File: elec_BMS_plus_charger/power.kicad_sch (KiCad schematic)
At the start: 42 parts, among them J1 Conn_01x02, J13 Dynamixel-3, J14 Dynamixel-3, J2 JST SH, J7 JST SH, Q1 Q_NMOS_DGS, Q2 Q_NMOS_DGS, U1 HY2120, U2 BQ25887RGE

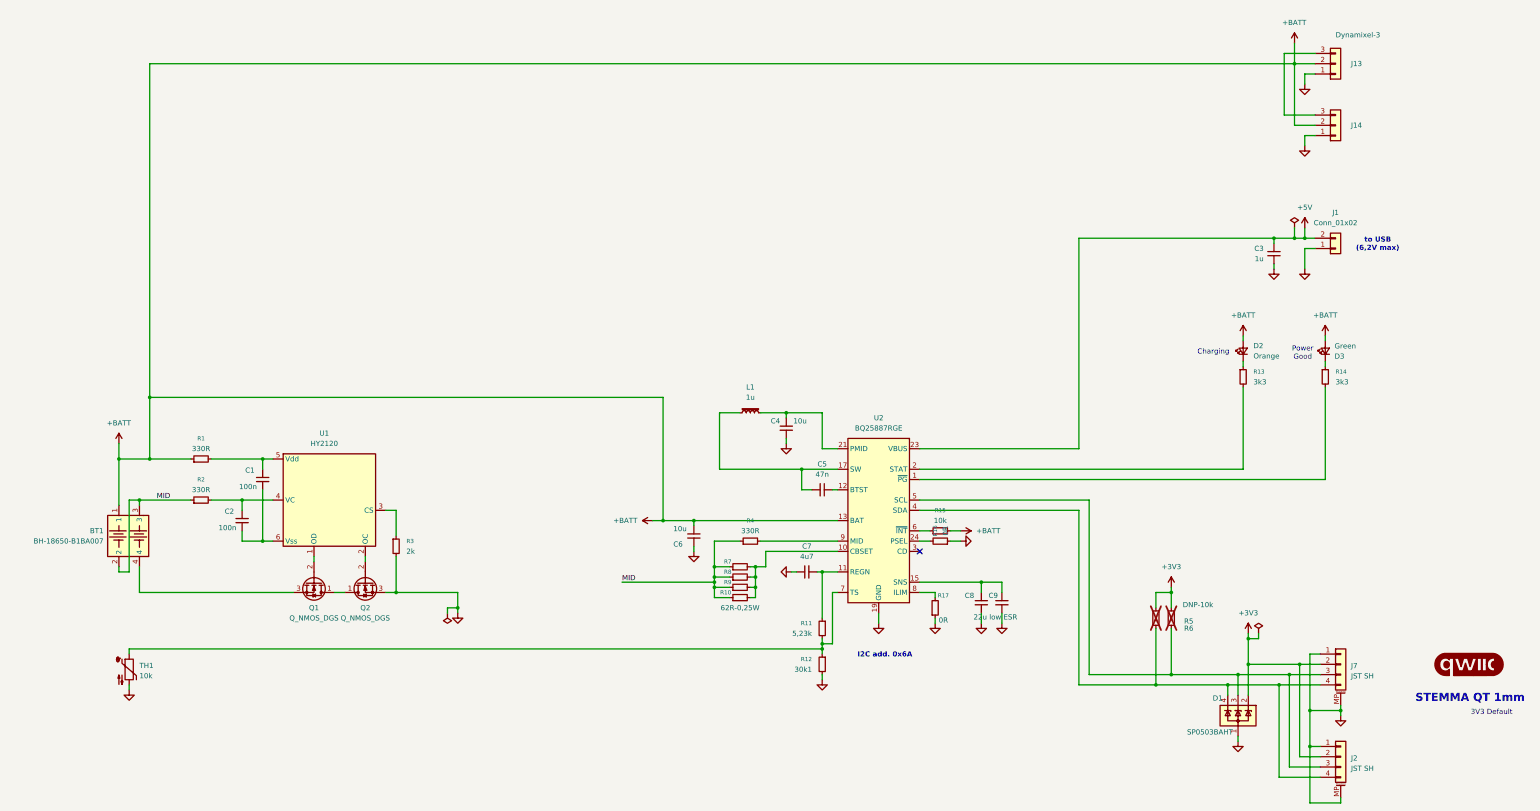
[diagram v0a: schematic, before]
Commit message: [update] BMS schematic DRC 0k.
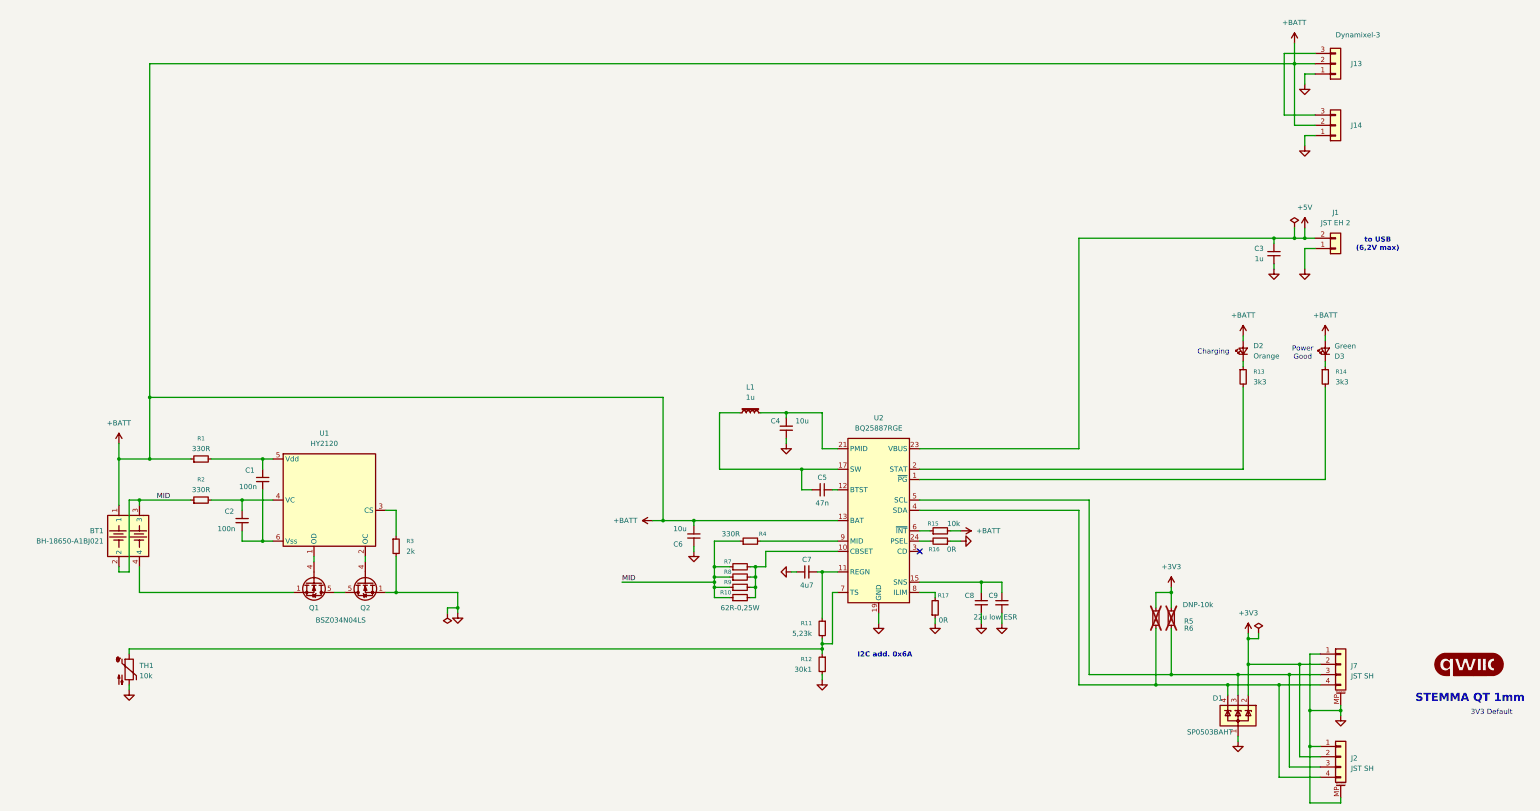
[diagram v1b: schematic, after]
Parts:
- removed Q1, Q2: Q_NMOS_DGS, symbol Transistor_FET:Q_NMOS_DGS
- added Q1, Q2: BSZ034N04LS, Library_Pollen:PQFN_3.3x3.3mm_-_PG-TDSON-8_FL, symbol Library_Pollen:BSZ034N04LS
- BT1: value BH-18650-B1BA007 -> BH-18650-A1BJ021; footprint LCSC_parts_lib:BAT-SMD_BH-18650-B1BA007 -> LCSC_parts_lib:BAT-TH_L77.0-W39.9_BH-18650-A1BJ021; LCSC Part C6937126 -> C20606804
- C3, L1: footprint (none) -> Capacitor_SMD:C_0402_1005Metric; LCSC Part (none) -> C52923
- C4, C6: footprint (none) -> Capacitor_SMD:C_0603_1608Metric; LCSC Part (none) -> C19702
- C5: footprint (none) -> Capacitor_SMD:C_0402_1005Metric; LCSC Part (none) -> C272875
- C7: footprint (none) -> Capacitor_SMD:C_0603_1608Metric; LCSC Part (none) -> C1705
- C8: footprint (none) -> Capacitor_SMD:C_0805_2012Metric; LCSC Part (none) -> C5674
- C9: value 22u -> 22u low ESR; footprint (none) -> Capacitor_SMD:C_0805_2012Metric; LCSC Part (none) -> C5674
- D2: footprint (none) -> LED_SMD:LED_0603_1608Metric; LCSC Part (none) -> C84269
- J1: value Conn_01x02 -> JST EH 2; footprint (none) -> Connector_JST:JST_EH_B2B-EH-A_1x02_P2.50mm_Vertical; LCSC Part (none) -> C160262
- J2, J7: footprint Connector_JST:JST_SH_SM04B-SRSS-TB_1x04-1MP_P1.00mm_Horizontal -> Connector_JST:JST_SH_BM04B-SRSS-TB_1x04-1MP_P1.00mm_Vertical; LCSC Part C160404 -> C160390
- R1, R2, R4: LCSC Part (none) -> C25104
- R10, R7, R8, R9: footprint (none) -> Resistor_SMD:R_1206_3216Metric; LCSC Part (none) -> C3013271
- R11: footprint (none) -> Resistor_SMD:R_0402_1005Metric; LCSC Part (none) -> C2933105
- R12: footprint (none) -> Resistor_SMD:R_0402_1005Metric; LCSC Part (none) -> C2998131
- R13, R14: footprint (none) -> Resistor_SMD:R_0402_1005Metric; LCSC Part (none) -> C25890
- R15, TH1: footprint (none) -> Resistor_SMD:R_0402_1005Metric; LCSC Part (none) -> C2906861
- R3: footprint (none) -> Resistor_SMD:R_0402_1005Metric; LCSC Part (none) -> C2909344
- R5, R6: LCSC Part C25744 -> (none)
- U2: LCSC Part (none) -> C2761614; Man. (none) -> TI; Man. Ref. (none) -> BQ25887RGER
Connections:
- net GND: now also Q2.1 (S)
- net at BT1.4: now also Q1.1 (S)
- net at U1.2 (OC): now also Q2.4 (G)
- net at U1.1 (OD): now also Q1.4 (G)
- new net: Q1.5 (D), Q2.5 (D)

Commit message: [update] Mechanical adaptations.
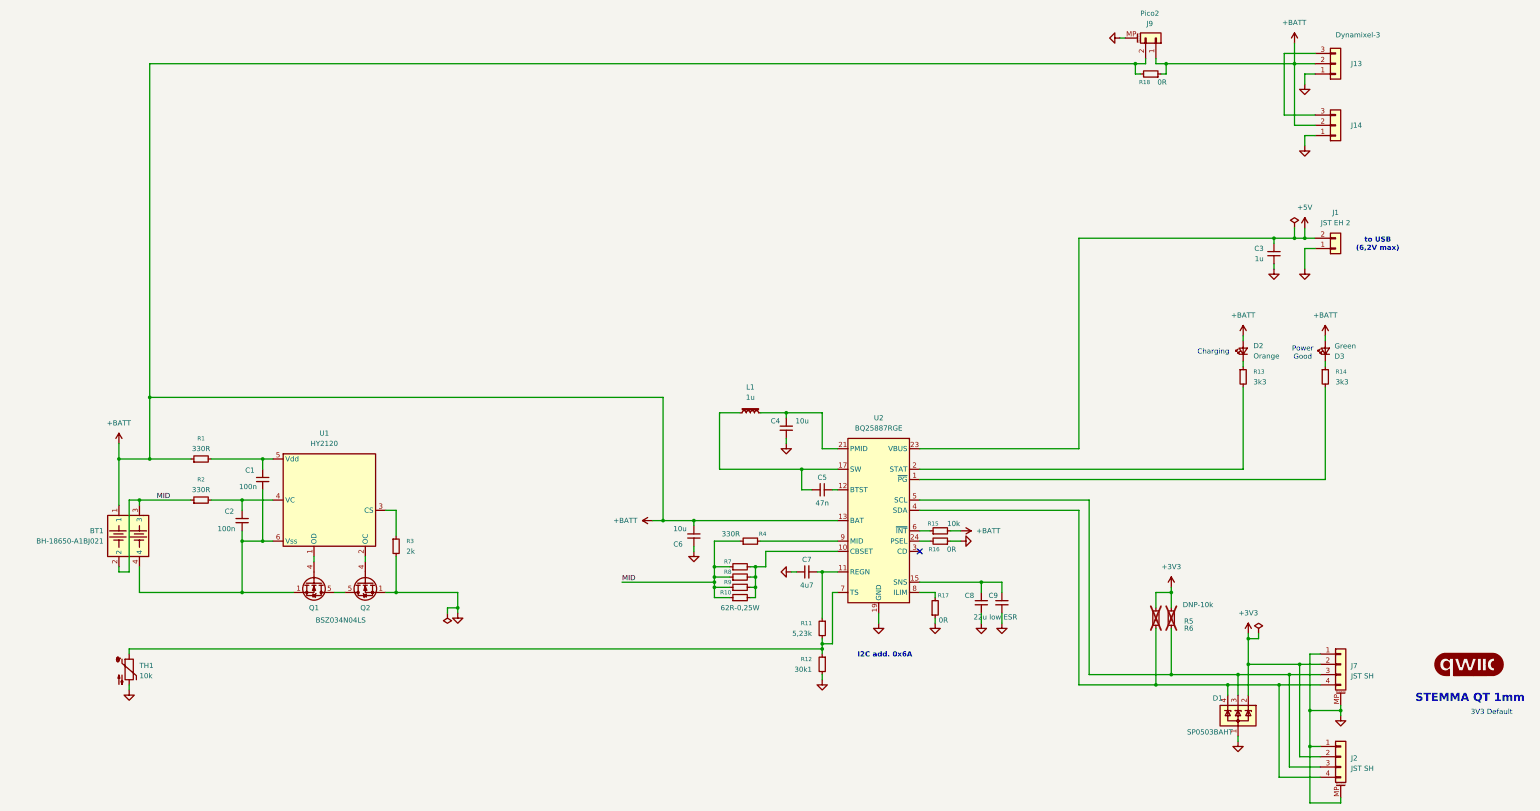
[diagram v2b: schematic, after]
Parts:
- added J9: Pico2, Connector_Molex:Molex_PicoBlade_53047-0210_1x02_P1.25mm_Vertical, symbol Connector_Generic_MountingPin:Conn_01x02_MountingPin
- added R18: 0R, Resistor_SMD:R_0603_1608Metric, symbol Device:R_Small
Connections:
- net +BATT: now also J9.1 (Pin_1), J9.2 (Pin_2), R18.1, R18.2
- net GND: now also J9.MP (MountPin)
- net at BT1.4, Q1.1 (S): now also C1.2, C2.2, U1.6 (Vss)

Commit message: [update] BMS+charger DRC OK
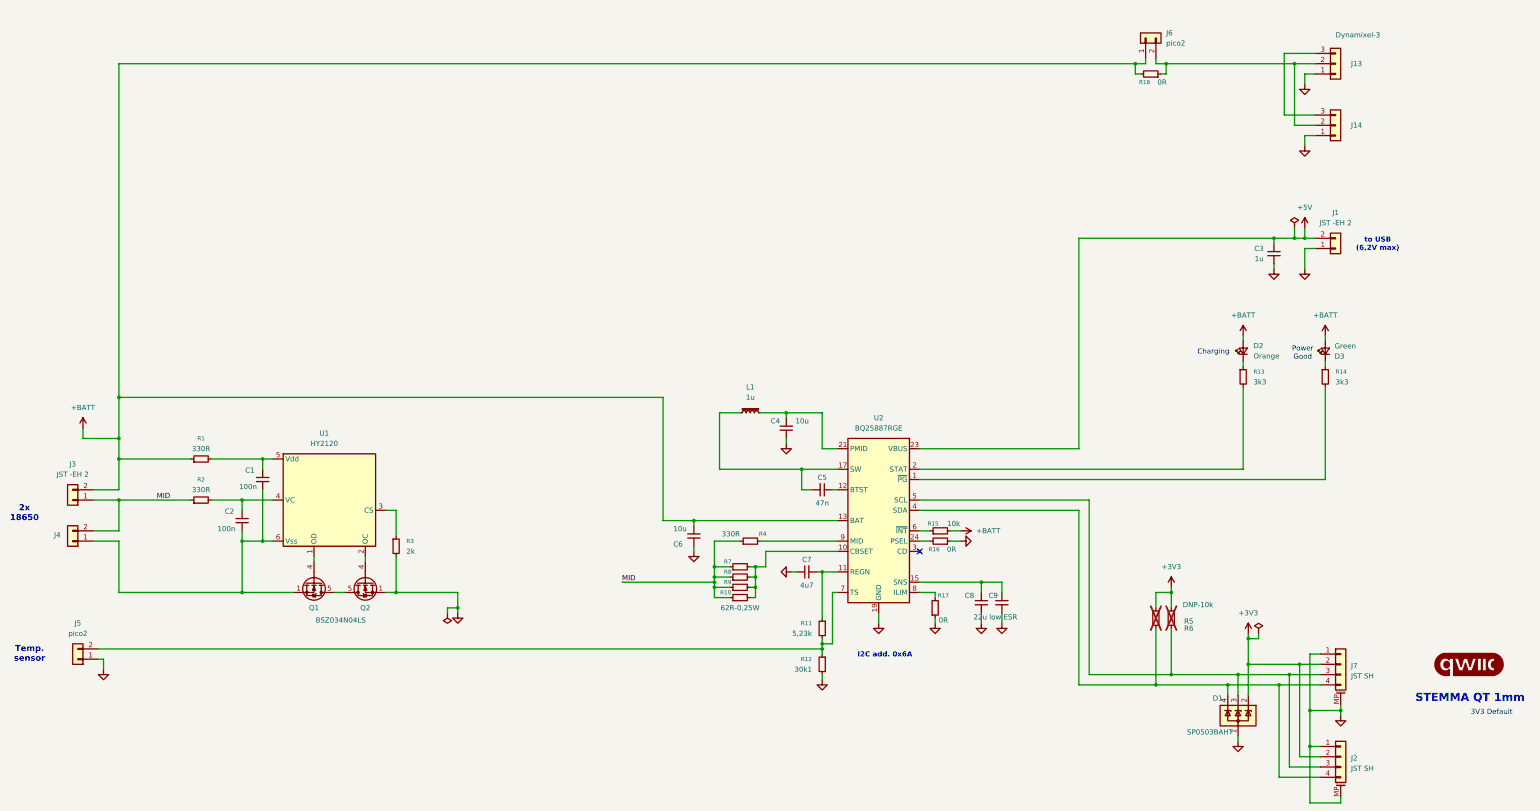
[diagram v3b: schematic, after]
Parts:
- removed BT1: BH-18650-A1BJ021, LCSC_parts_lib:BAT-TH_L77.0-W39.9_BH-18650-A1BJ021, symbol Library_Pollen:BH-18650-B1BA007
- removed J9: Pico2, Connector_Molex:Molex_PicoBlade_53047-0210_1x02_P1.25mm_Vertical, symbol Connector_Generic_MountingPin:Conn_01x02_MountingPin
- removed TH1: 10k, Resistor_SMD:R_0402_1005Metric, symbol Device:Thermistor_NTC
- added J3, J4: JST -EH 2, Connector_JST:JST_EH_B2B-EH-A_1x02_P2.50mm_Vertical, symbol Connector_Generic:Conn_01x02
- added J5, J6: pico2, Library_Pollen:Molex_PicoBlade_53047-0210_1x02_P1.25mm_Vertical, symbol Connector_Generic:Conn_01x02
- J1: value JST EH 2 -> JST -EH 2
- L1: footprint Capacitor_SMD:C_0402_1005Metric -> Inductor_SMD:L_6.3x6.3_H3; LCSC Part C52923 -> C5189744
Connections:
- net +BATT: now also J3.2 (Pin_2), J6.1 (Pin_1); no longer J13.2 (Pin_2), J14.2 (Pin_2), R18.1
- net GND: now also J5.1 (Pin_1)
- net MID: now also J3.1 (Pin_1), J4.2 (Pin_2)
- net at C1.2, C2.2, Q1.1 (S)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: now also J4.1 (Pin_1)
- net at R11.2, R12.1, U2.7 (TS): now also J5.2 (Pin_2)
- new net: J13.2 (Pin_2), J14.2 (Pin_2), J6.2 (Pin_2), R18.1
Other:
- note added: "2x 18650"
- note added: "Temp. sensor"
